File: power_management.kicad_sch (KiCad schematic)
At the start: 19 parts, among them IC3 MCP73831T-2ATI_OT, IC4 AP2112K-3.3TRG1, J2 USB_C_Receptacle_USB2.0_14P

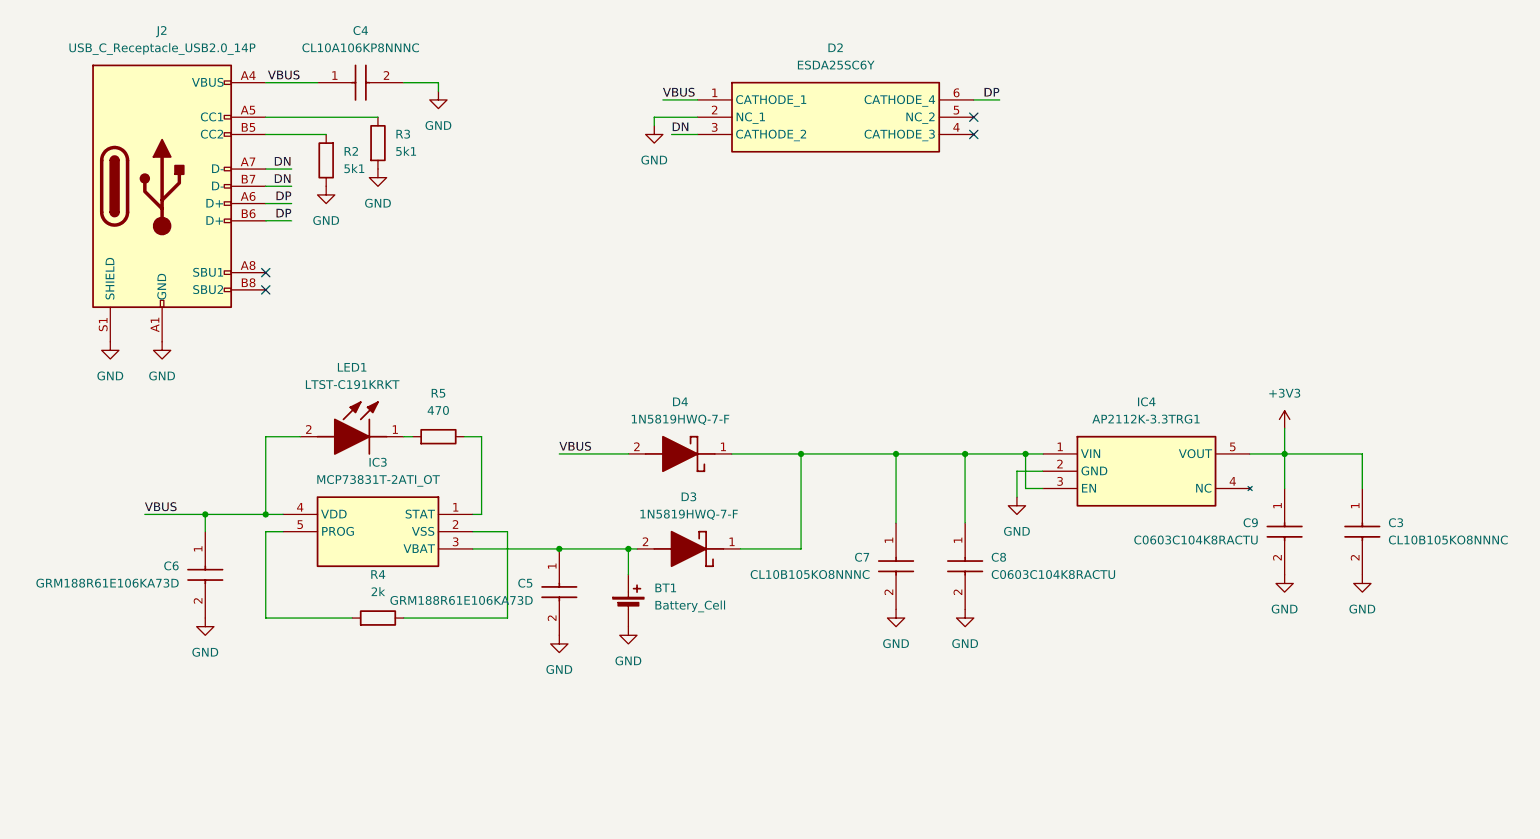
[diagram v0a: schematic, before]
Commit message: cleaned up and annotated the schematic
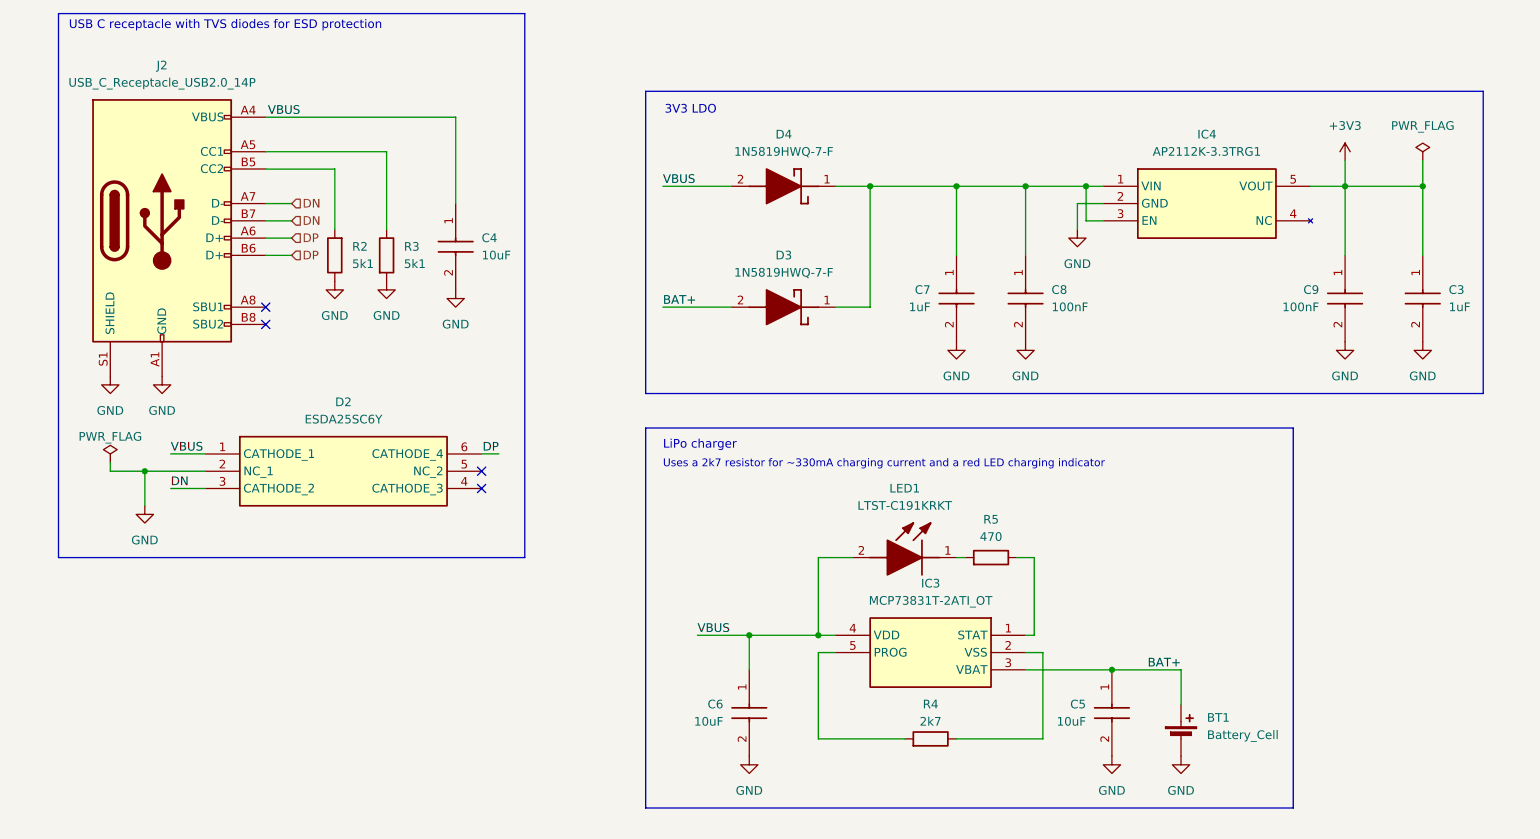
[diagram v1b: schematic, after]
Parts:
- C3, C7: value CL10B105KO8NNNC -> 1uF
- C4: value CL10A106KP8NNNC -> 10uF
- C5, C6: value GRM188R61E106KA73D -> 10uF
- C8, C9: value C0603C104K8RACTU -> 100nF
- R4: value 2k -> 2k7
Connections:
- net BAT+: now reaches BT1.1 (+), C5.1, D3.2 (A), IC3.3 (VBAT)
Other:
- note added: "3V3 LDO"
- note added: "LiPo charger"
- note added: "USB C receptacle with TVS diodes for ESD protection"
- note added: "Uses a 2k7 resistor for ~330mA charging current and a red LED charging indicator"
- moved on the sheet: BT1, C3, C4, C5, C6, C7, C8, C9, D2, D3, D4, IC3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

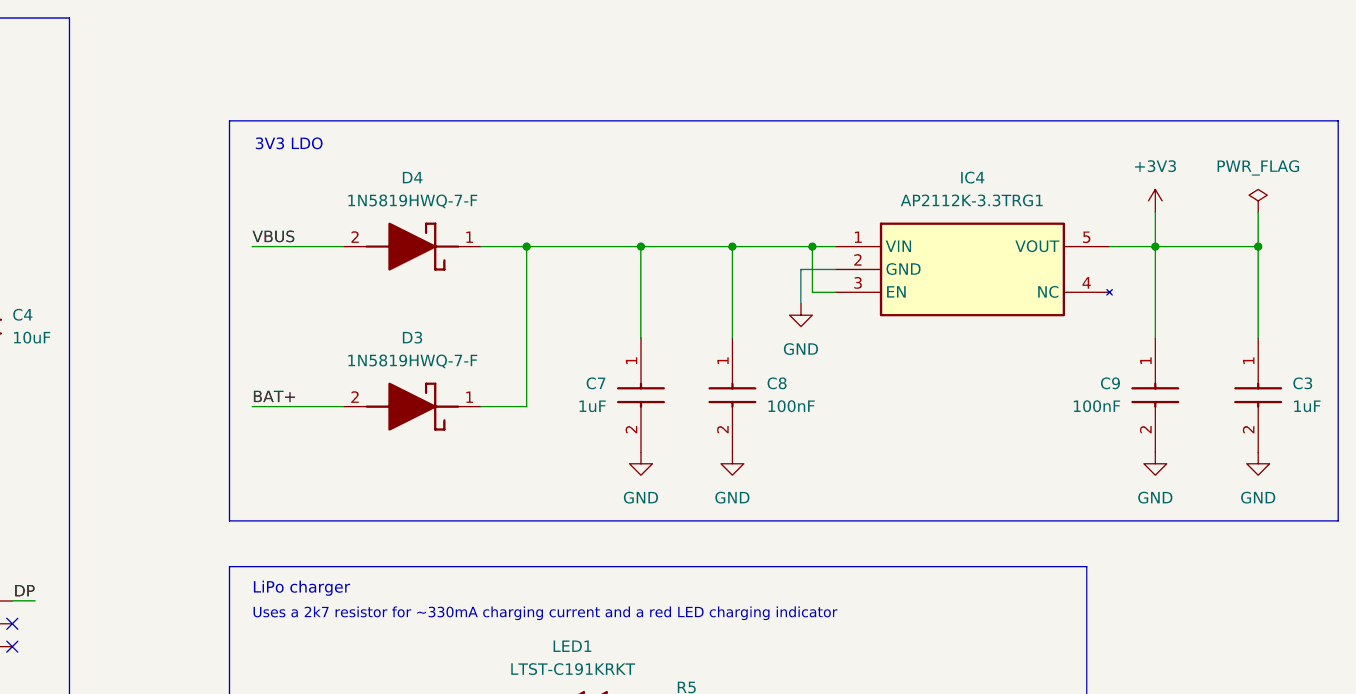
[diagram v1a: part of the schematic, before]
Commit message: modified the LDO circuit by adding a p-mosfet high side switch
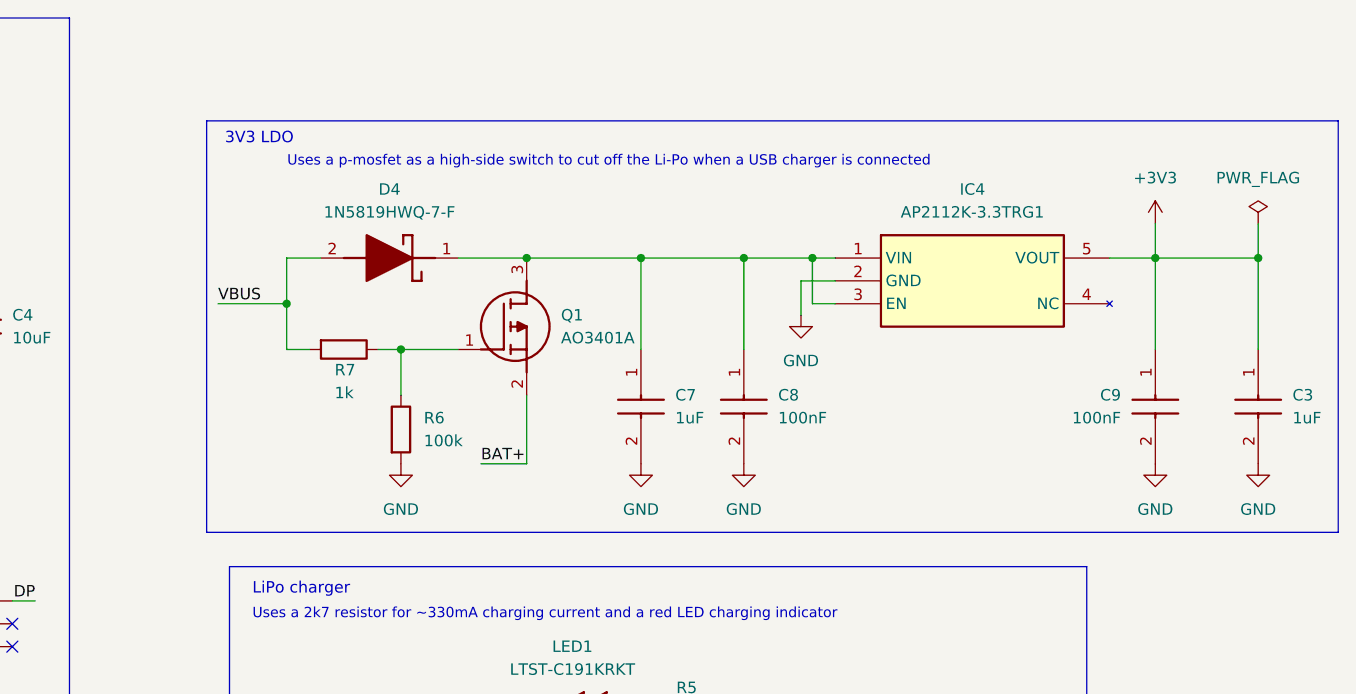
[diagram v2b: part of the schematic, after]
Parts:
- removed D3: 1N5819HWQ-7-F, LifeCounter-Footprints:Diodes-Inc_SOD3716X145M, symbol LifeCounter-Symbols:1N5819HWQ-7-F
- added Q1: AO3401A, LifeCounter-Footprints:Alpha&Omega_SOT95P280X125-3M, symbol LifeCounter-Symbols:AO3401A
- added R6: 100k, Resistor_SMD:R_0603_1608Metric_Pad0.98x0.95mm_HandSolder, symbol Device:R
- added R7: 1k, Resistor_SMD:R_0603_1608Metric_Pad0.98x0.95mm_HandSolder, symbol Device:R
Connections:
- net BAT+: now also Q1.2 (S)
- net GND: now also R6.2
- net VBUS: now also R7.2
- net at C7.1, C8.1, D4.1 (K)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: now also Q1.3 (D)
- new net: Q1.1 (G), R6.1, R7.1
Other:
- note added: "Uses a p-mosfet as a high-side switch to cut off the Li-Po when a USB charger is connected"
- moved on the sheet: C3, C7, C8, C9, D4, IC4

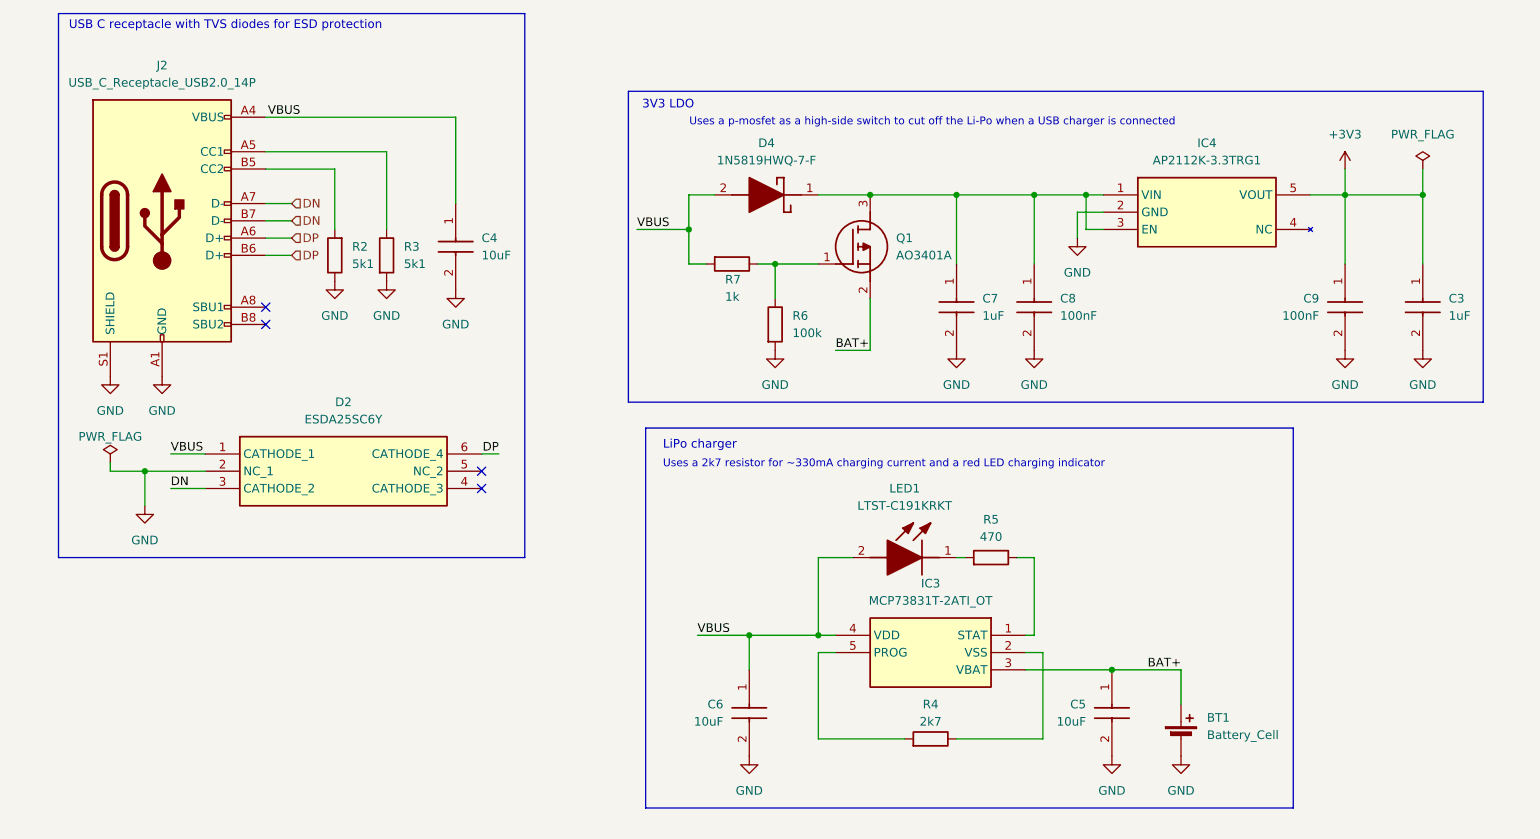
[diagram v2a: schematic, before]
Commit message: labeled the FPC tape connector (LCD) pins
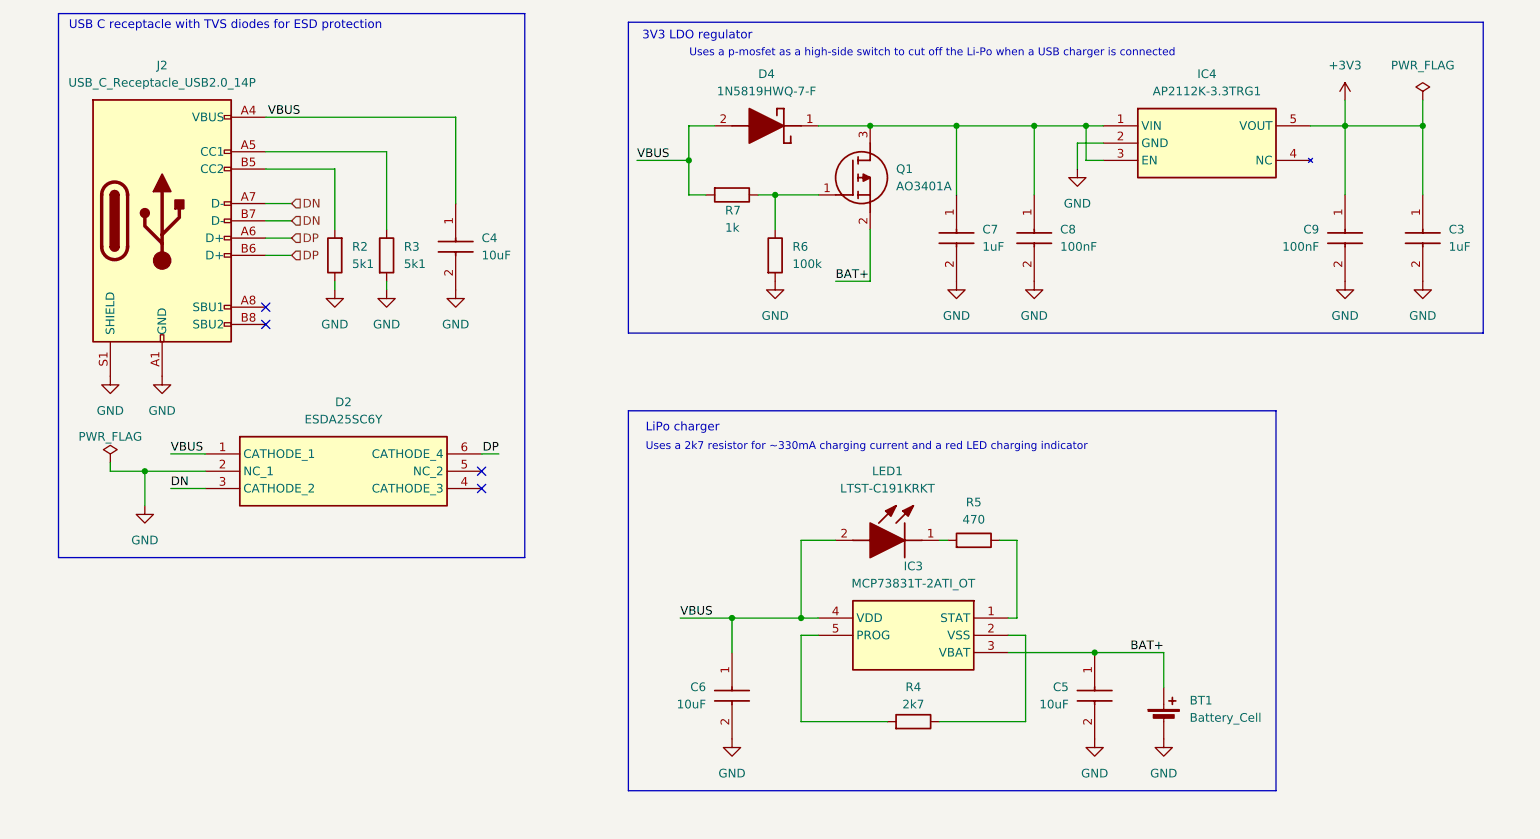
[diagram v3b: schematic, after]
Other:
- note added: "3V3 LDO regulator"
- note removed: "3V3 LDO"
- moved on the sheet: BT1, C3, C5, C6, C7, C8, C9, D4, IC3, IC4, LED1, Q1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

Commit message: fix: added a 2ohm resistor to prevent voltage spikes on USB-C input (LC)
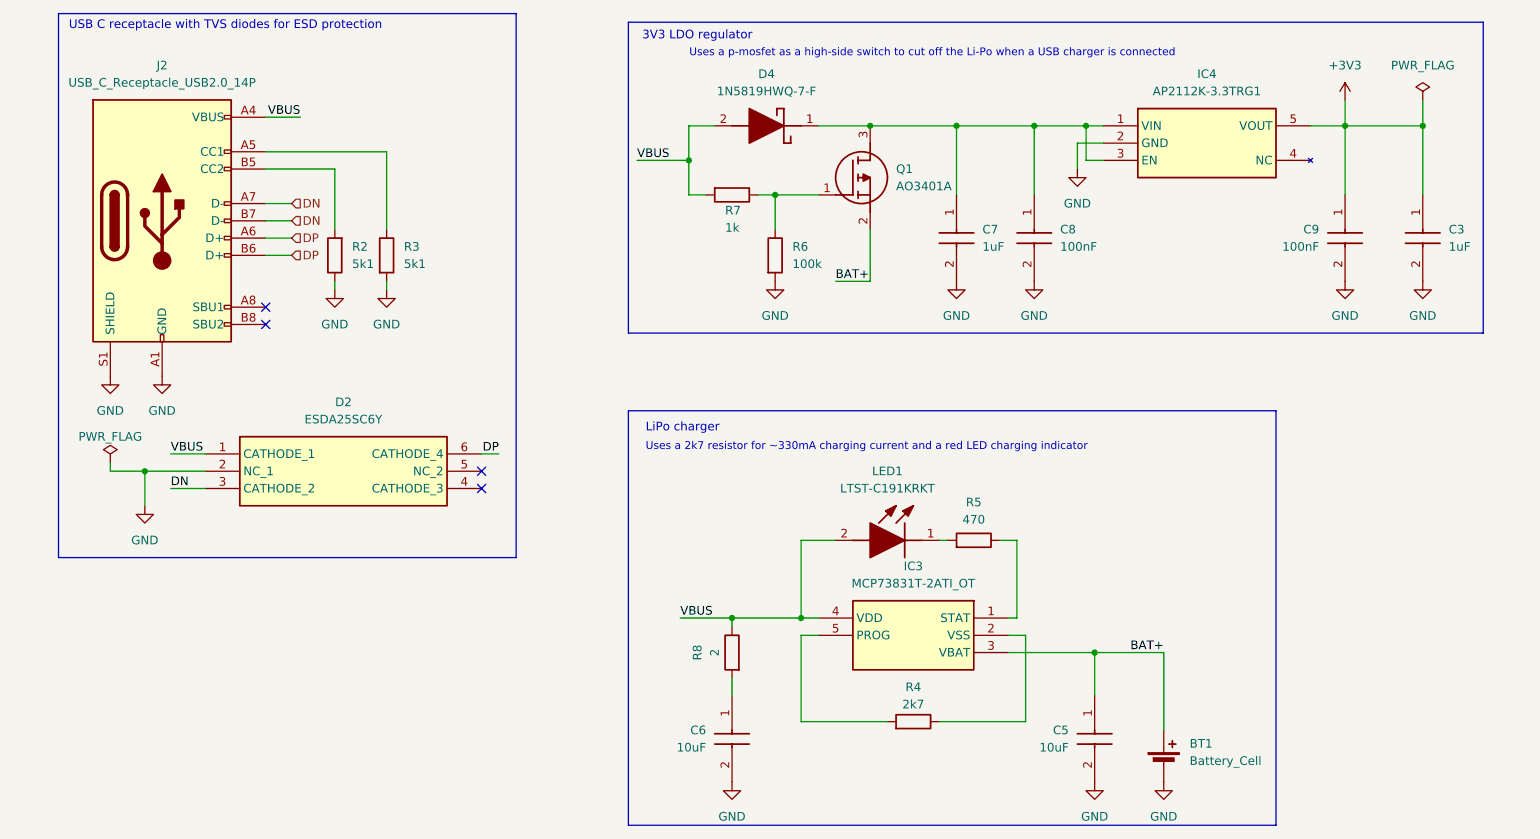
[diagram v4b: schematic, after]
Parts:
- removed C4: 10uF, LifeCounter-Footprints:Samsung_CAPC1608X90M, symbol LifeCounter-Symbols:CL10A106KP8NNNC
- added R8: 2, Resistor_SMD:R_0603_1608Metric_Pad0.98x0.95mm_HandSolder, symbol Device:R
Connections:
- net VBUS: now also R8.1; no longer C6.1
- new net: C6.1, R8.2
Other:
- moved on the sheet: BT1, C5, C6

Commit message: fixed: changedthe orientation of the AO3401A mosfet
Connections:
- net BAT+: now also Q1.3 (D); no longer Q1.2 (S)
- net at C7.1, C8.1, D4.1 (K)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: now also Q1.2 (S); no longer Q1.3 (D)
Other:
- moved on the sheet: Q1
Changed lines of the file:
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@@
 	(wire
 		(pts
-			(xy 142.24 58.42) (xy 142.24 50.8)
+			(xy 142.24 58.42) (xy 142.24 55.88)
 		)
 		(stroke
@@
 	(wire
 		(pts
+			(xy 142.24 35.56) (xy 154.94 35.56)
+		)
+		(stroke
+			(width 0)
+			(type default)
+		)
+	)
+	(wire
+		(pts
 			(xy 71.12 59.69) (xy 71.12 58.42)
 		)
@@
 	(wire
 		(pts
+			(xy 142.24 40.64) (xy 142.24 35.56)
+		)
+		(stroke
+			(width 0)
+			(type default)
+		)
+	)
+	(wire
+		(pts
 			(xy 165.1 110.49) (xy 165.1 123.19)
 		)
@@
 	(wire
 		(pts
-			(xy 142.24 35.56) (xy 134.62 35.56)
+			(xy 134.62 35.56) (xy 142.24 35.56)
 		)
 		(stroke
@@
 	(wire
 		(pts
-			(xy 142.24 35.56) (xy 154.94 35.56)
-		)
-		(stroke
-			(width 0)
-			(type default)
-		)
-	)
-	(wire
-		(pts
 			(xy 172.72 38.1) (xy 172.72 41.91)
 		)
@@
 		(lib_id "LifeCounter-Symbols:AO3401A")
 		(at 134.62 45.72 0)
+		(mirror x)
 		(unit 1)
 		(exclude_from_sim no)
@@
 		(on_board yes)
 		(dnp no)
-		(fields_autoplaced yes)
 		(property "Reference" "Q1"
-			(at 146.05 41.9099 0)
+			(at 146.05 46.9899 0)
 			(effects
 				(font
@@
 		)
 		(property "Value" "AO3401A"
-			(at 146.05 44.4499 0)
+			(at 146.05 49.5299 0)
 			(effects
 				(font
@@
 		)
 		(property "Footprint" "LifeCounter-Footprints:Alpha&Omega_SOT95P280X125-3M"
-			(at 146.05 144.45 0)
+			(at 146.05 -53.01 0)
 			(effects
 				(font
@@
 		)
 		(property "Datasheet" "http://www.aosmd.com/pdfs/datasheet/AO3401A.pdf"
-			(at 146.05 244.45 0)
+			(at 146.05 -153.01 0)
 			(effects
 				(font
@@
 		)
 		(property "Height" "1.25"
-			(at 146.05 444.45 0)
+			(at 146.05 -353.01 0)
 			(effects
 				(font
@@
 		)
 		(property "TME Electronic Components Part Number" ""
-			(at 146.05 544.45 0)
+			(at 146.05 -453.01 0)
 			(effects
 				(font
@@
 		)
 		(property "TME Electronic Components Price/Stock" ""
-			(at 146.05 644.45 0)
+			(at 146.05 -553.01 0)
 			(effects
 				(font
@@
 		)
 		(property "Manufacturer_Name" "Alpha & Omega Semiconductors"
-			(at 146.05 744.45 0)
+			(at 146.05 -653.01 0)
 			(effects
 				(font
@@
 		)
 		(property "Manufacturer_Part_Number" "AO3401A"
-			(at 146.05 844.45 0)
+			(at 146.05 -753.01 0)
 			(effects
 				(font
@@
 		)
 		(instances
-			(project ""
+			(project "LifeCounter"
 				(path "/4fcff061-b5b1-4f40-9b81-6bf0aa8b3dad/ac1f3ae2-c9f5-46ef-b6fa-0a2fe52bf2e0"
 					(reference "Q1")
